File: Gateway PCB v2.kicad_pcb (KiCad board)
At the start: 4 copper layers, 79.9 x 39.5 mm, 109 parts, among them J1 Conn_Coaxial, J2 Conn_01x04_Pin, J3 Conn_02x03_Odd_Even, J4 Conn_01x03_Pin, U6 TPS7A91, U7 TLV62568ADRL, X1 TG2016SMN 32.0000M-TCGNNMB

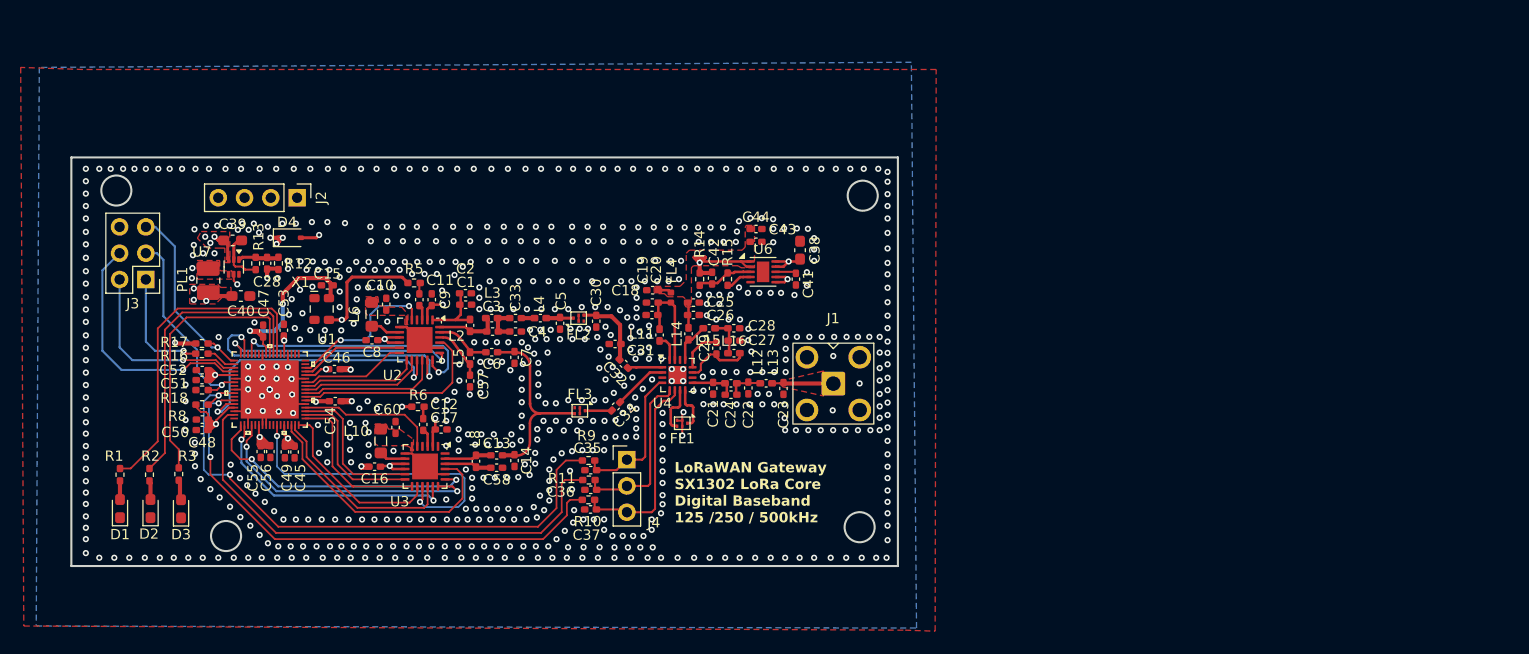
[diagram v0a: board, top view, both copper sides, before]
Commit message: re route sky
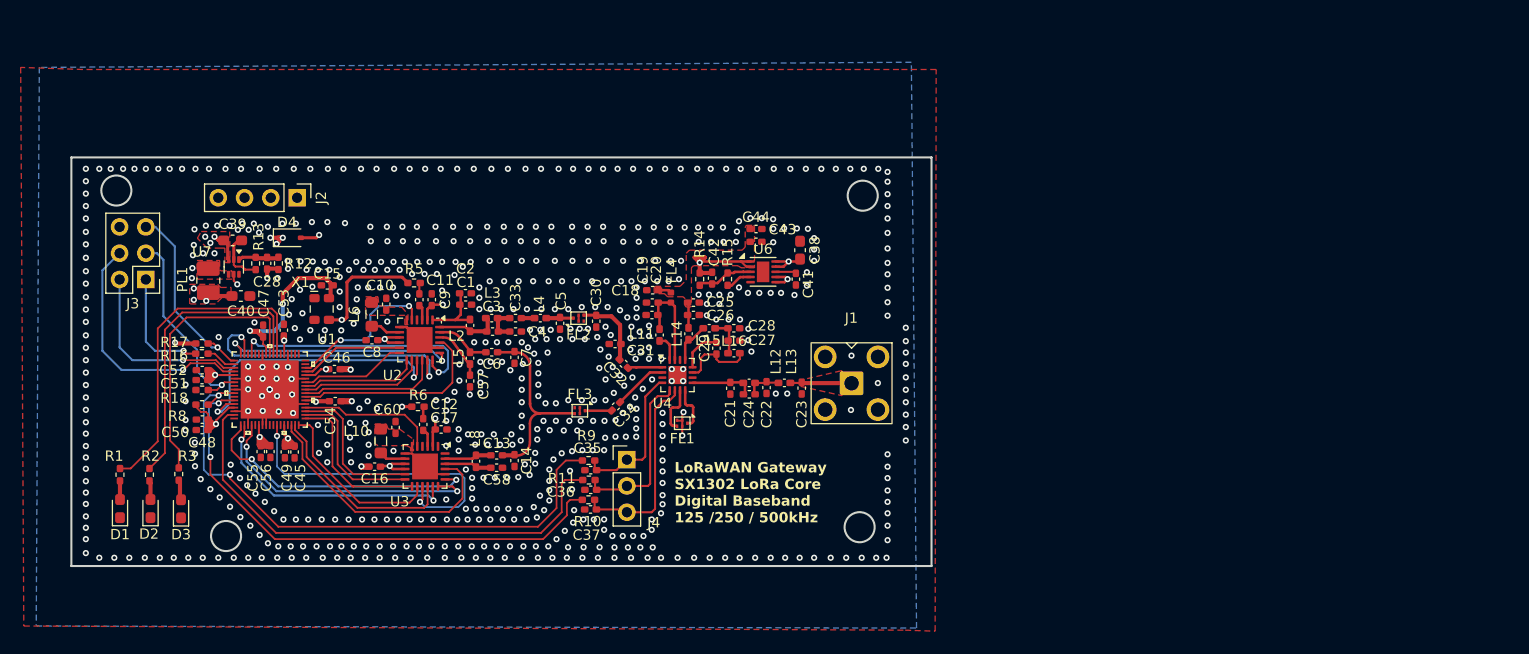
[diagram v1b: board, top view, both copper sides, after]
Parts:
- moved C24 1.76 mm to (79.3, 87.6)
- moved C22 1.76 mm to (81.0, 87.0)
- moved C23 1.76 mm to (84.4, 87.0)
- moved J1 1.76 mm to (89.2, 86.5)
- moved L13 1.76 mm to (82.7, 86.5)
- moved L12 1.76 mm to (79.3, 86.5)
- moved C21 1.66 mm to (77.5, 87.0)
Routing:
- net Net-(U4-ANT): track 4.47 -> 6.20 mm
- net Net-(U4-TX_IN): track 6.75 -> 7.42 mm
- net GND: vias 706 -> 661
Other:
- board size 79.9 x 39.5 mm -> 83.2 x 39.5 mm

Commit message: UpDate
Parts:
- added NT1: NetTie_2, NetTie:NetTie-2_SMD_Pad0.5mm, F.Cu at (86.5, 85.1)
- added NT2: NetTie_2, NetTie:NetTie-2_SMD_Pad0.5mm, F.Cu at (86.5, 88.9)
- added NT3: NetTie_2, NetTie:NetTie-2_SMD_Pad0.5mm, F.Cu at (86.0, 70.3)
- added NT4: NetTie_2, NetTie:NetTie-2_SMD_Pad0.5mm, F.Cu at (23.0, 70.9)
- added NT5: NetTie_2, NetTie:NetTie-2_SMD_Pad0.5mm, F.Cu at (86.0, 103.5)
- moved D1 47.0 mm to (54.0, 67.9), turned to -90 degrees
- moved R1 42.6 mm to (52.0, 69.1), turned to 0 degrees
- moved D2 40.7 mm to (48.3, 68.0), turned to -90 degrees
- moved R2 36.1 mm to (46.2, 69.2), turned to 0 degrees
- moved D3 35.7 mm to (42.8, 68.1), turned to -90 degrees
- moved R3 31.0 mm to (40.7, 69.1), turned to 0 degrees
- moved J2 10.1 mm to (25.6, 68.5)
- moved J3 3.17 mm to (20.5, 79.6)
- moved J1 2.82 mm to (92.0, 86.5)
- moved C21 2.09 mm to (79.6, 87.0)
- moved C22 2.09 mm to (83.1, 87.0)
- moved C24 2.09 mm to (81.4, 87.6)
- moved L12 2.09 mm to (81.4, 86.5)
- moved C23 2.09 mm to (86.5, 87.0)
- moved L13 2.09 mm to (84.8, 86.5)
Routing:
- net Net-(U1-GPIO[3]): track 27.1 -> 18.3 mm, vias 0 -> 2
- net Net-(U1-GPIO[4]): track 29.0 -> 22.9 mm, vias 0 -> 2
- net GND2: track 0.00 -> 5.00 mm
- net Net-(U1-GPIO[5]): track 32.1 -> 27.6 mm, vias 0 -> 2
- net 3.3V: track 94.4 -> 98.5 mm
- net EX_HOST_MISO: track 11.3 -> 8.40 mm
- net EX_HOST_MOSI: track 18.5 -> 15.6 mm
- net EX_HOST_RESET: track 20.0 -> 17.3 mm
- net EX_HOST_SCK: track 24.2 -> 21.8 mm
- net 5V: track 17.3 -> 19.6 mm
- net EX_HOST_CSN: track 18.6 -> 16.4 mm
- net Net-(U4-ANT): track 6.20 -> 8.29 mm
- net Net-(J1-In): track 6.15 -> 7.01 mm
- net SX1302_CSD: track 55.2 -> 56.0 mm
- net RADIO_B_IQ_3: track 26.1 -> 26.7 mm
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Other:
- board size 83.2 x 39.5 mm -> 83.6 x 39.8 mm

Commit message: Fail Save
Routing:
- net EX_HOST_MISO: track 8.40 -> 10.0 mm
- net GND: track 50.0 -> 49.5 mm, vias 466 -> 564

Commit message: Increse size
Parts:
- moved NT4 0.73 mm to (22.3, 70.9)
- moved J3 0.38 mm to (20.1, 79.6)
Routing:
- net 3.3V: track 98.0 -> 134.6 mm
- net EX_HOST_SCK: track 22.2 -> 23.4 mm
- net EX_HOST_MOSI: track 15.7 -> 16.3 mm
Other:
- board size 83.6 x 39.8 mm -> 84.4 x 39.8 mm

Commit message: Fail Save 2
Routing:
- net EX_HOST_SCK: track 23.4 -> 24.4 mm
- net GND2: track 5.04 -> 5.83 mm
- net Net-(D4-K): track 86.0 -> 86.5 mm, vias 9 -> 8
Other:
- outline, holes or cut-outs redrawn

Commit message: Fail Save 3
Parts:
- J3: footprint Connector_PinHeader_2.54mm:PinHeader_2x03_P2.54mm_Vertical -> Connector_PinHeader_2.54mm:PinHeader_1x06_P2.54mm_Vertical
- moved C27 47.9 mm to (125.5, 77.2)
- moved C28 47.9 mm to (125.4, 76.0)
- moved C29 47.9 mm to (123.8, 77.9)
- moved L15 47.9 mm to (123.0, 76.0)
- moved L16 47.9 mm to (125.4, 78.4)
- moved NT2 47.0 mm to (133.2, 83.6)
- moved J2 47.0 mm to (72.3, 64.1)
- moved C38 46.9 mm to (131.0, 69.7)
- moved C1 46.9 mm to (98.7, 75.0)
- moved C47 46.9 mm to (79.1, 77.5)
- moved C51 46.9 mm to (73.2, 82.3)
- moved C53 46.9 mm to (81.1, 77.4)
- moved C54 46.9 mm to (86.1, 84.3)
- moved C57 46.9 mm to (99.1, 82.4)
- moved L10 46.9 mm to (90.5, 88.2)
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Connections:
- J3 pad 1: EX_HOST_MISO -> EX_HOST_SCK
- J3 pad 3: EX_HOST_RESET -> EX_HOST_MISO
- J3 pad 4: EX_HOST_SCK -> EX_HOST_RESET
- J3 pad 6: unconnected-(J3-Pin_6-Pad6) -> GND
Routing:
- net EX_HOST_SCK: track 24.4 -> 11.9 mm
- net EX_HOST_MOSI: track 16.3 -> 11.0 mm
- net Net-(J1-In): track 7.01 -> 11.8 mm
- net Net-(U4-ANT): track 8.29 -> 4.19 mm
- net EX_HOST_MISO: track 10.2 -> 7.63 mm
- net GND2: track 5.83 -> 3.83 mm
- net Net-(U4-PA_OUT): track 3.97 -> 5.71 mm
- net EX_HOST_CSN: track 16.5 -> 14.8 mm
- net Net-(U4-TX_IN): track 7.42 -> 8.90 mm
- net GND: track 49.5 -> 50.8 mm, vias 564 -> 605
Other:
- board size 84.4 x 39.8 mm -> 85 x 41 mm
- board text added: "3.3V"
- board text added: "5V"
- board text added: "CSD"
- board text added: "CSN"
- board text added: "GND"
- board text added: "MISO"
- board text added: "MOSI"
- board text added: "PA_ON"
- board text added: "RST"
- board text added: "TXTX"

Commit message: Fail Save 4
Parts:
- moved NT2 0.06 mm to (133.2, 83.7)
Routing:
- net GND: track 50.8 -> 52.8 mm, vias 605 -> 607
- net 1.2V: track 70.4 -> 68.9 mm

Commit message: Success
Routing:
- net EX_HOST_MISO: track 7.63 -> 10.1 mm
- net EX_HOST_MOSI: track 11.0 -> 12.5 mm
- net 3.3V: track 135.0 -> 135.9 mm
- net RADIOB_RESET: track 31.2 -> 31.9 mm
- net EX_HOST_CSN: track 14.8 -> 15.3 mm
- net EX_HOST_SCK: track 11.9 -> 12.5 mm
